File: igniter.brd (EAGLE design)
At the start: 65 x 56 mm, 19 parts, among them X1 RASPI_BOARD_B+#_H, X3 5566-4-RIGHTANGLE

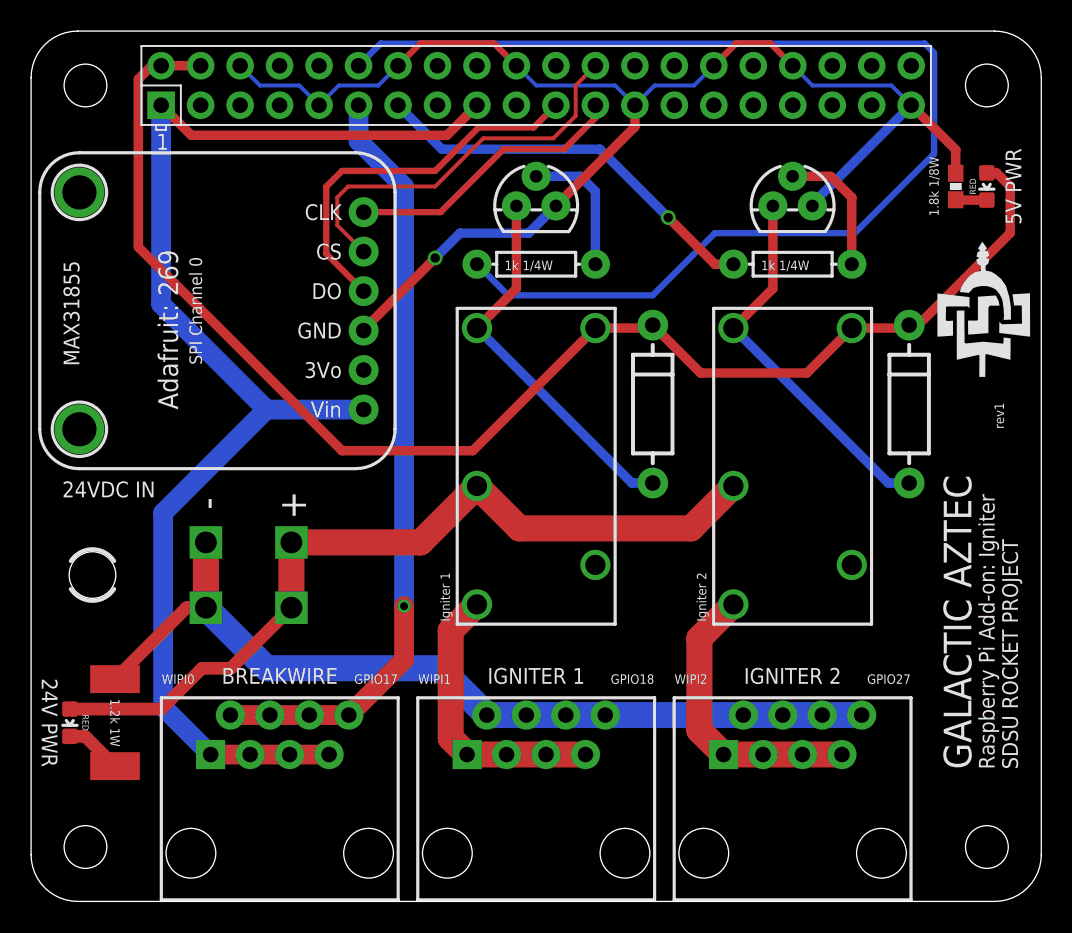
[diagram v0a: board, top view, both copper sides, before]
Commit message: Power connector and resistor updates. Added PCB images (generated by OSHPark). Added README.md.
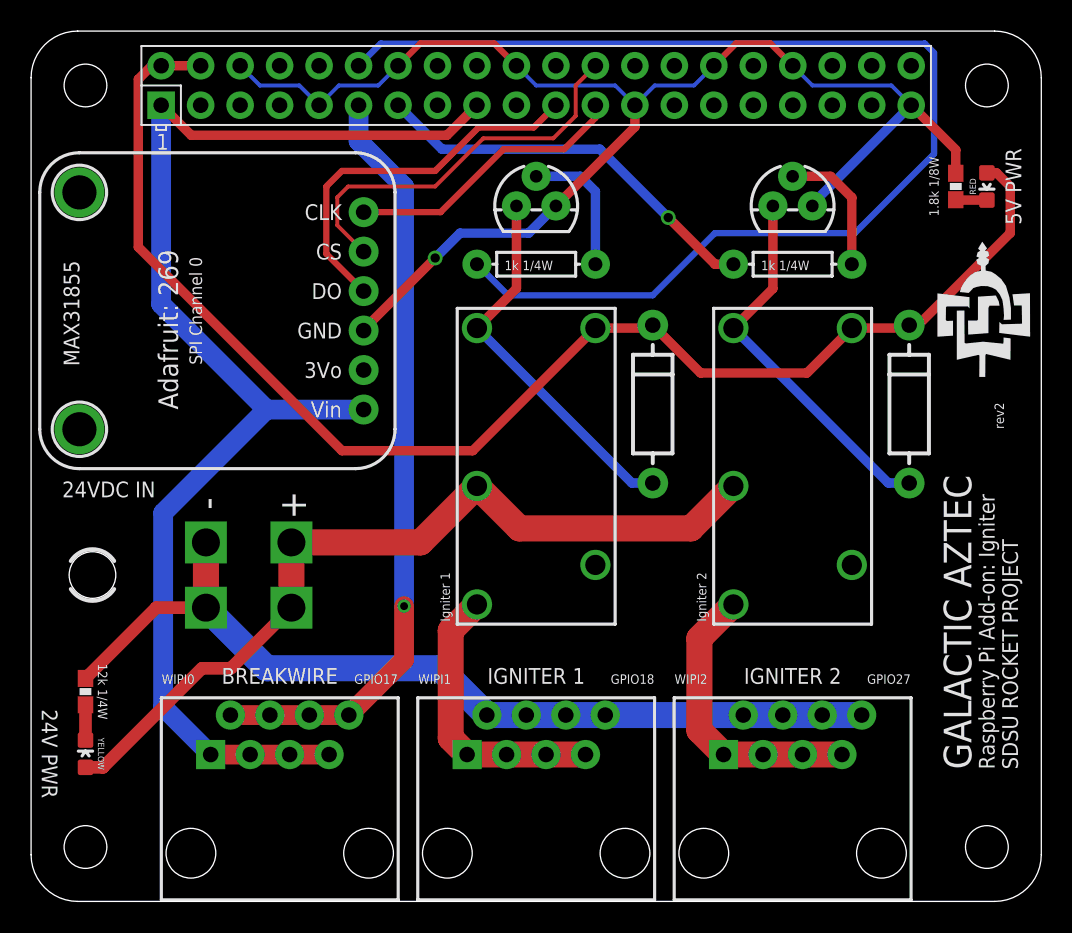
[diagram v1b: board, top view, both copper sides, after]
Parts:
- removed X3: 5566-4-RIGHTANGLE, SDSURocket-BreakoutBoards:5566-4
- added X2: 5566-4-RIGHTANGLE, SDSURocket-Connectors:5566-4
- D3: value RED -> YELLOW
- R3: value 1.2k 1W -> 12k 1/4W; device SparkFun-Resistors:R2512 -> SparkFun-Resistors:0603-RES
- moved R3 2.76 mm to (3.50, 13.5)
- moved D3 2.24 mm to (3.50, 9.50), turned to 0 degrees
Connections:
- net 24V: now also X2.3, X2.4; no longer X3.3, X3.4
- net GND2: now also X2.1, X2.2; no longer X3.1, X3.2
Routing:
- net GND2: track 57.0 -> 58.9 mm
- net N$3: track 3.70 -> 2.27 mm
- net 24V: track 53.4 -> 53.9 mm
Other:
- board text added: "rev2"
- board text removed: "rev1"
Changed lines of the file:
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@@
 <plain>
 <text x="62.7" y="46" size="1.016" layer="25" font="vector" ratio="10" rot="R90" align="top-center">5V PWR</text>
-<text x="1.7" y="11.5" size="1.016" layer="25" font="vector" ratio="10" rot="SR270" align="top-center">24V PWR</text>
+<text x="1.7" y="9.5" size="1.016" layer="25" font="vector" ratio="10" rot="SR270" align="top-center">24V PWR</text>
 <text x="32.5" y="14" size="1.016" layer="25" font="vector" ratio="12" align="bottom-center">IGNITER 1</text>
 <text x="49" y="14" size="1.016" layer="25" font="vector" ratio="12" align="bottom-center">IGNITER 2</text>
@@
 <text x="62" y="8.5" size="1.016" layer="25" font="vector" ratio="10" rot="R90">Raspberry Pi Add-on: Igniter</text>
 <text x="63.5" y="8.5" size="1.016" layer="25" font="vector" rot="R90">SDSU ROCKET PROJECT</text>
-<text x="62.6" y="30.4" size="0.6096" layer="25" font="vector" rot="R90">rev1</text>
+<text x="62.6" y="30.4" size="0.6096" layer="25" font="vector" rot="R90">rev2</text>
 <text x="11" y="38" size="0.8128" layer="25" font="vector" rot="R270" align="top-center">SPI Channel 0</text>
 <polygon width="0" layer="25">
@@
 </element>
 <element name="U$1" library="SDSURocket-BreakoutBoards" package="ADAFRUIT-MAX31855" value="ADAFRUIT-MAX31855-BREAKOUT" x="12" y="38" smashed="yes" rot="R90"/>
-<element name="X3" library="SDSURocket-BreakoutBoards" package="5566-4" value="5566-4-RIGHTANGLE" x="14" y="21" smashed="yes" rot="R270">
+<element name="D3" library="SparkFun-LED" package="LED-0603" value="YELLOW" x="3.5" y="9.5" smashed="yes">
+<attribute name="VALUE" x="4.3" y="9.5" size="0.4064" layer="25" font="vector" rot="SR270" align="bottom-center"/>
+</element>
+<element name="D4" library="SparkFun-LED" package="LED-0603" value="RED" x="61.5" y="46" smashed="yes" rot="R180">
+<attribute name="VALUE" x="60.8" y="46" size="0.4064" layer="25" font="vector" rot="R90" align="bottom-center"/>
+</element>
+<element name="R3" library="SparkFun-Resistors" package="0603-RES" value="12k 1/4W" x="3.5" y="13.5" smashed="yes" rot="R90">
+<attribute name="VALUE" x="4.6" y="13.5" size="0.6096" layer="25" font="vector" rot="SR270" align="center"/>
+</element>
+<element name="R4" library="SparkFun-Resistors" package="0603-RES" value="1.8k 1/8W" x="59.5" y="46" smashed="yes" rot="R90">
+<attribute name="VALUE" x="58.4" y="46" size="0.6096" layer="25" font="vector" rot="R90" align="bottom-center"/>
+</element>
+<element name="X2" library="SDSURocket-Connectors" package="5566-4" value="5566-4-RIGHTANGLE" x="14" y="21" smashed="yes" rot="R270">
 <attribute name="OC_NEWARK" value="unknown" x="14" y="21" size="1.778" layer="27" rot="R270" display="off"/>
 <attribute name="MPN" value="" x="14" y="21" size="1.778" layer="27" rot="R270" display="off"/>
 <attribute name="MF" value="" x="14" y="21" size="1.778" layer="27" rot="R270" display="off"/>
 <attribute name="OC_FARNELL" value="unknown" x="14" y="21" size="1.778" layer="27" rot="R270" display="off"/>
-</element>
-<element name="D3" library="SparkFun-LED" package="LED-0603" value="RED" x="2.5" y="11.5" smashed="yes" rot="R180">
-<attribute name="VALUE" x="3.3" y="11.5" size="0.4064" layer="25" font="vector" rot="SR270" align="bottom-center"/>
-</element>
-<element name="D4" library="SparkFun-LED" package="LED-0603" value="RED" x="61.5" y="46" smashed="yes" rot="R180">
-<attribute name="VALUE" x="60.8" y="46" size="0.4064" layer="25" font="vector" rot="R90" align="bottom-center"/>
-</element>
-<element name="R3" library="SparkFun-Resistors" package="R2512" value="1.2k 1W" x="5.4" y="11.5" smashed="yes" rot="R90">
-<attribute name="VALUE" x="5.4" y="11.5" size="0.6096" layer="25" font="vector" rot="SR270" align="center"/>
-</element>
-<element name="R4" library="SparkFun-Resistors" package="0603-RES" value="1.8k 1/8W" x="59.5" y="46" smashed="yes" rot="R90">
-<attribute name="VALUE" x="58.4" y="46" size="0.6096" layer="25" font="vector" rot="R90" align="bottom-center"/>
 </element>
 </elements>
@@
 <contactref element="RELAY3" pad="2"/>
 <contactref element="RELAY4" pad="2"/>
-<contactref element="X3" pad="3"/>
-<contactref element="X3" pad="4"/>
 <contactref element="D3" pad="A"/>
 <wire x1="16.75" y1="23.1" x2="16.75" y2="18.9" width="1.6764" layer="1"/>
@@
 <wire x1="31.42" y1="24" x2="42.46" y2="24" width="1.6764" layer="1"/>
 <wire x1="45.19" y1="26.73" x2="42.46" y2="24" width="1.6764" layer="1"/>
-<wire x1="2.5" y1="12.377" x2="8.377" y2="12.377" width="0.8128" layer="1"/>
-<wire x1="8.377" y1="12.377" x2="11" y2="15" width="0.8128" layer="1"/>
-<wire x1="11" y1="15" x2="12.85" y2="15" width="0.8128" layer="1"/>
-<wire x1="12.85" y1="15" x2="16.75" y2="18.9" width="0.8128" layer="1"/>
+<contactref element="X2" pad="3"/>
+<contactref element="X2" pad="4"/>
+<wire x1="3.5" y1="8.623" x2="4.623" y2="8.623" width="0.8128" layer="1"/>
+<wire x1="4.623" y1="8.623" x2="11" y2="15" width="0.8128" layer="1"/>
+<wire x1="16.75" y1="18.9" x2="12.85" y2="15" width="0.8128" layer="1"/>
+<wire x1="12.85" y1="15" x2="11" y2="15" width="0.8128" layer="1"/>
 </signal>
 <signal name="N$5">
@@
 <contactref element="RJ45-2" pad="6"/>
 <contactref element="RJ45-2" pad="8"/>
-<contactref element="X3" pad="1"/>
-<contactref element="X3" pad="2"/>
 <contactref element="R3" pad="2"/>
 <wire x1="11.25" y1="23.1" x2="11.25" y2="18.9" width="1.6764" layer="1"/>
@@
 <wire x1="48.365" y1="11.99" x2="50.905" y2="11.99" width="1.6764" layer="16"/>
 <wire x1="50.905" y1="11.99" x2="53.445" y2="11.99" width="1.6764" layer="16"/>
-<wire x1="5.4" y1="14.3" x2="10" y2="18.9" width="0.8128" layer="1"/>
-<wire x1="10" y1="18.9" x2="11.25" y2="18.9" width="0.8128" layer="1"/>
+<contactref element="X2" pad="1"/>
+<contactref element="X2" pad="2"/>
+<wire x1="3.5" y1="14.35" x2="8.05" y2="18.9" width="0.8128" layer="1"/>
+<wire x1="8.05" y1="18.9" x2="11.25" y2="18.9" width="0.8128" layer="1"/>
 </signal>
 <signal name="IGN1">
@@
 <contactref element="D3" pad="C"/>
 <contactref element="R3" pad="1"/>
-<wire x1="5.4" y1="8.7" x2="3.477" y2="10.623" width="0.8128" layer="1"/>
-<wire x1="3.477" y1="10.623" x2="2.5" y2="10.623" width="0.8128" layer="1"/>
+<wire x1="3.5" y1="12.65" x2="3.5" y2="10.377" width="0.8128" layer="1"/>
 </signal>
 <signal name="N$4">
